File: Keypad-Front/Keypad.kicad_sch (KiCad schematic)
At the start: 64 parts, among them J1 RTC STEMMA QT, J3 JST-PH 6, J4 JST-PH 6, J5 JST-PH 8, J6 EXP QWIIC, J7 TOUCH QWIIC, U1 DS3231MZ, U2 LM1117-3.3, U3 CAP1214

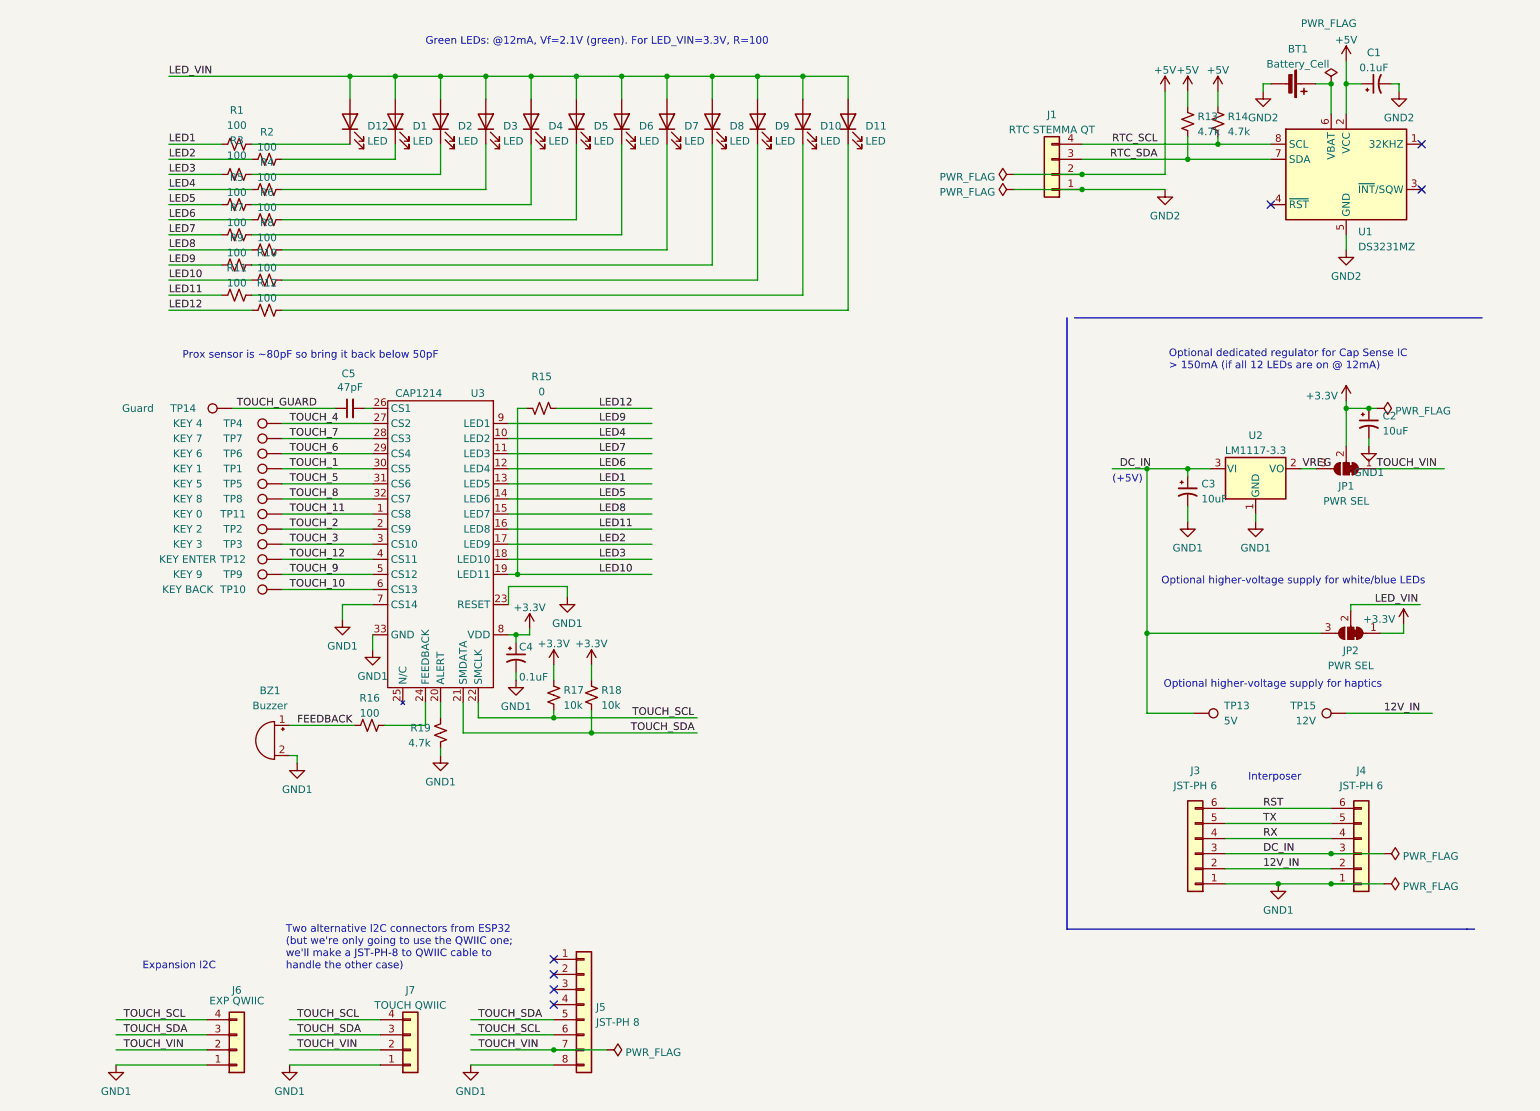
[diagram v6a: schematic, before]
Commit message: Fix some errors in original boards; add RFID functionality
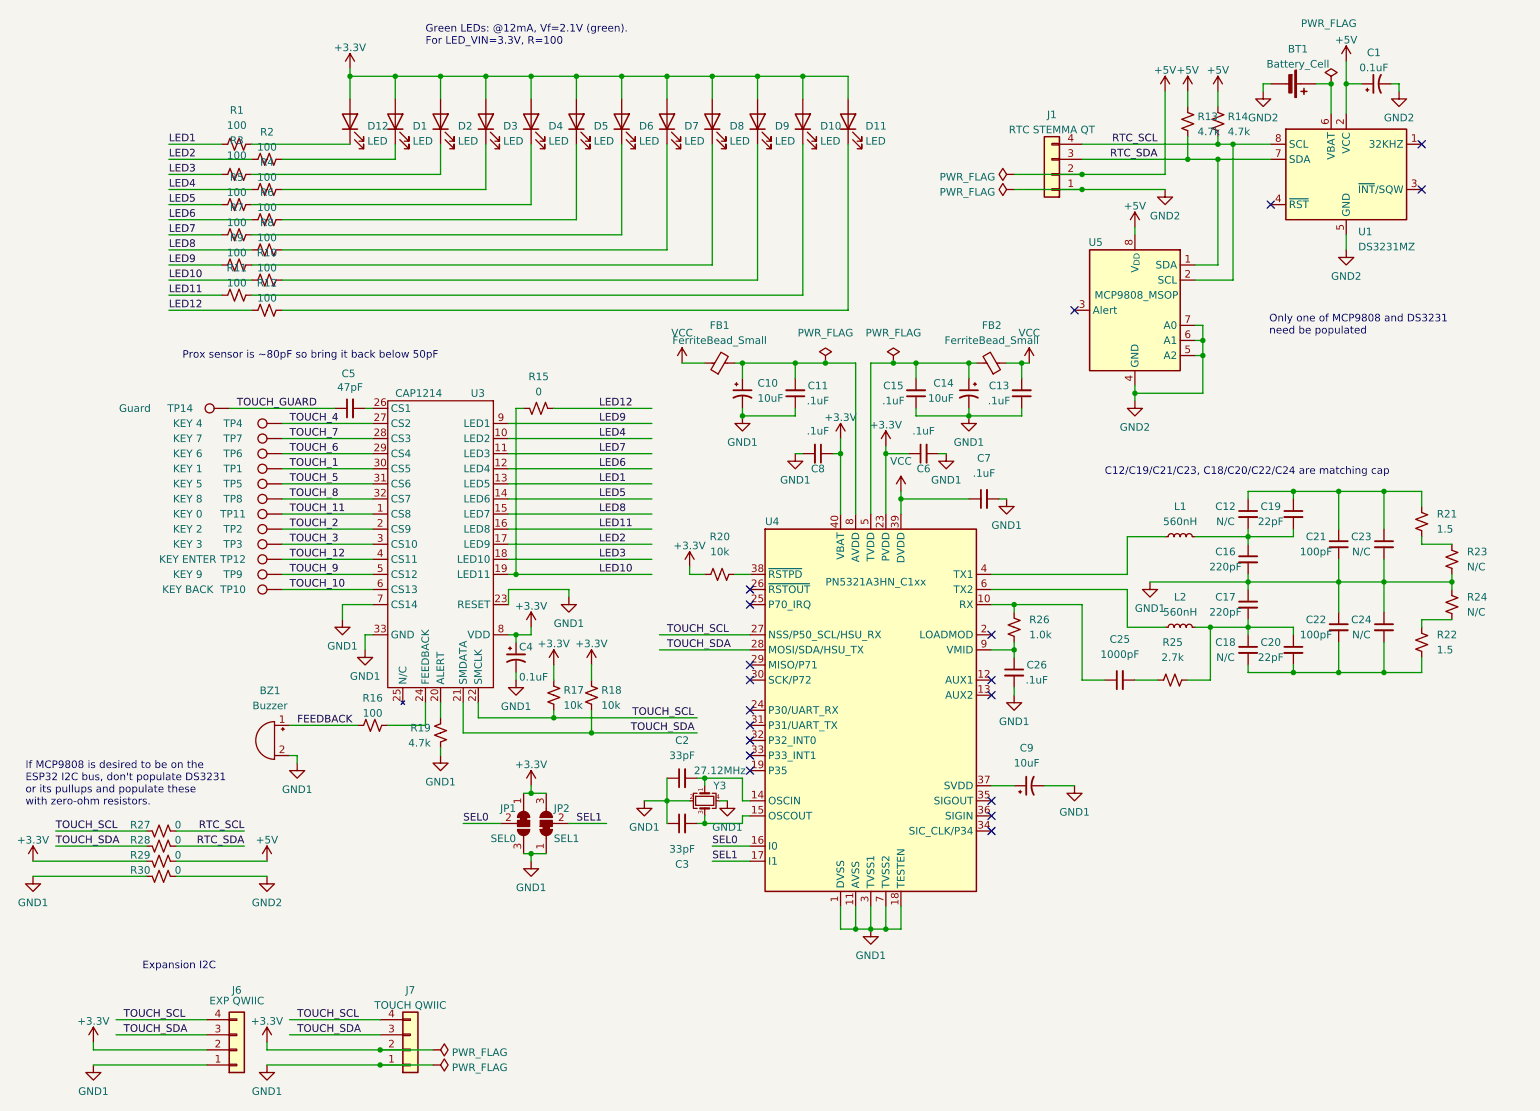
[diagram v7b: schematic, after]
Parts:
- removed C2, C3: 10uF, Capacitor_SMD:C_0805_2012Metric_Pad1.18x1.45mm_HandSolder, symbol Device:C_Polarized_Small_US
- removed J3, J4: JST-PH 6, Keypad:JST-PH-6-SMD, symbol Connector_Generic:Conn_01x06
- removed J5: JST-PH 8, symbol Connector_Generic:Conn_01x08
- removed TP13: 5V, TestPoint:TestPoint_Pad_2.0x2.0mm, symbol Connector:TestPoint
- removed TP15: 12V, TestPoint:TestPoint_Pad_2.0x2.0mm, symbol Connector:TestPoint
- removed U2: LM1117-3.3, Package_TO_SOT_SMD:SOT-223-3_TabPin2, symbol Regulator_Linear:LM1117-3.3
- added C10, C14, C9: 10uF, Capacitor_SMD:C_0805_2012Metric_Pad1.18x1.45mm_HandSolder, symbol Device:C_Polarized_Small_US
- added C11, C13, C15, C26, C6, C7, C8: .1uF, Capacitor_SMD:C_0805_2012Metric_Pad1.18x1.45mm_HandSolder, symbol Device:C_Small
- added C12, C18, C23, C24: N/C, Capacitor_SMD:C_0805_2012Metric_Pad1.18x1.45mm_HandSolder, symbol Device:C_Small
- added C16, C17: 220pF, Capacitor_SMD:C_0805_2012Metric_Pad1.18x1.45mm_HandSolder, symbol Device:C_Small
- added C19, C20: 22pF, Capacitor_SMD:C_0805_2012Metric_Pad1.18x1.45mm_HandSolder, symbol Device:C_Small
- added C2, C3: 33pF, Capacitor_SMD:C_0805_2012Metric_Pad1.18x1.45mm_HandSolder, symbol Device:C_Small
- added C21, C22: 100pF, Capacitor_SMD:C_0805_2012Metric_Pad1.18x1.45mm_HandSolder, symbol Device:C_Small
- added C25: 1000pF, Capacitor_SMD:C_0805_2012Metric_Pad1.18x1.45mm_HandSolder, symbol Device:C_Small
- added FB1, FB2: FerriteBead_Small, Resistor_SMD:R_0805_2012Metric_Pad1.20x1.40mm_HandSolder, symbol Device:FerriteBead_Small
- added L1, L2: 560nH, Inductor_SMD:L_0805_2012Metric_Pad1.15x1.40mm_HandSolder, symbol Device:L_Small
- added R20: 10k, Resistor_SMD:R_0805_2012Metric_Pad1.20x1.40mm_HandSolder, symbol Device:R_Small_US
- added R21, R22: 1.5, Resistor_SMD:R_0805_2012Metric_Pad1.20x1.40mm_HandSolder, symbol Device:R_Small_US
- added R23, R24: N/C, Jumper:SolderJumper-2_P1.3mm_Bridged_Pad1.0x1.5mm, symbol Device:R_Small_US
- added R25: 2.7k, Resistor_SMD:R_0805_2012Metric_Pad1.20x1.40mm_HandSolder, symbol Device:R_Small_US
- added R26: 1.0k, Resistor_SMD:R_0805_2012Metric_Pad1.20x1.40mm_HandSolder, symbol Device:R_Small_US
- added R27, R28, R29, R30: 0, Resistor_SMD:R_0805_2012Metric_Pad1.20x1.40mm_HandSolder, symbol Device:R_Small_US
- added U4: PN5321A3HN_C1xx, Package_DFN_QFN:HVQFN-40-1EP_6x6mm_P0.5mm_EP4.1x4.1mm, symbol RF_NFC:PN5321A3HN_C1xx
- added U5: MCP9808_MSOP, Package_SO:MSOP-8_3x3mm_P0.65mm, symbol Sensor_Temperature:MCP9808_MSOP
- added Y3: 27.12MHz, Crystal:Crystal_SMD_TXC_7M-4Pin_3.2x2.5mm_HandSoldering, symbol Device:Crystal_GND24_Small
- JP1: value PWR SEL -> SEL0; footprint Jumper:SolderJumper-3_P1.3mm_Bridged12_RoundedPad1.0x1.5mm -> Jumper:SolderJumper-3_P1.3mm_Bridged12_Pad1.0x1.5mm
- JP2: value PWR SEL -> SEL1; footprint Jumper:SolderJumper-3_P1.3mm_Bridged12_RoundedPad1.0x1.5mm -> Jumper:SolderJumper-3_P1.3mm_Bridged12_Pad1.0x1.5mm
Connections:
- net DC_IN is gone; now on net GND1: JP2.3 (B)
- net VREG is gone; now on net +3.3V: JP1.3 (B)
- net +3.3V: now also D1.2 (A), D10.2 (A), D11.2 (A), D12.2 (A), D2.2 (A), D3.2 (A), D4.2 (A), D5.2 (A), D6.2 (A), D7.2 (A), D8.2 (A), D9.2 (A), J6.2 (Pin_2), J7.2 (Pin_2), C6.1, C8.1, R20.1, R29.1, U4.23 (PVDD), U4.40 (VBAT); no longer JP1.2 (C)
- net +5V: now also R29.2, U5.8 (V_{DD})
- net GND1: now also JP1.1 (A), C10.2, C11.1, C13.1, C14.2, C15.1, C16.2, C17.1, C2.1, C21.2, C22.1, C23.2, C24.1, C26.2, C3.1, C6.2, C7.2, C8.2, C9.2, R23.1, R24.2, R30.1, U4.1 (DVSS), U4.11 (AVSS), U4.18 (TESTEN), U4.3 (TVSS1), U4.41 (AVSS), U4.7 (TVSS2), Y3.2, Y3.4
- net GND2: now also R30.2, U5.4 (GND), U5.5 (A2), U5.6 (A1), U5.7 (A0)
- net RTC_SCL: now also R27.2, U5.2 (SCL)
- net RTC_SDA: now also R28.2, U5.1 (SDA)
- net TOUCH_SCL: now also R27.1, U4.27 (NSS/P50_SCL/HSU_RX)
- net TOUCH_SDA: now also R28.1, U4.28 (MOSI/SDA/HSU_TX)
- removed net LED_VIN: D1.2 (A), D10.2 (A), D11.2 (A), D12.2 (A), D2.2 (A), D3.2 (A), D4.2 (A), D5.2 (A), D6.2 (A), D7.2 (A), D8.2 (A), D9.2 (A), JP2.2 (C)
- removed net TOUCH_VIN: J6.2 (Pin_2), J7.2 (Pin_2), JP1.1 (A)
- new net: C14.1, C15.2, FB2.2, U4.5 (TVDD)
- new net: C25.1, R26.2, U4.10 (RX)
- new net: C2.2, U4.14 (OSCIN), Y3.1
- new net: C3.2, U4.15 (OSCOUT), Y3.3
- new net: C9.1, U4.37 (SVDD)
- new net: R20.2, U4.38 (~{RSTPD})
- new net: L1.1, U4.4 (TX1)
- new net: L2.1, U4.6 (TX2)
- new net: C10.1, C11.2, FB1.2, U4.8 (AVDD)
- new net: C26.1, R26.1, U4.9 (VMID)
- new net: R21.1, R23.2
- new net: C12.1, C19.1, C21.1, C23.1, R21.2
- new net: C17.2, C18.1, C20.1, L2.2, R25.1
- new net: C25.2, R25.2
- new net: C12.2, C16.1, C19.2, L1.2
- new net: C18.2, C20.2, C22.2, C24.2, R22.1
- new net: R22.2, R24.1
- new net SEL0: JP2.2 (C), U4.16 (I0)
- new net SEL1: JP1.2 (C), U4.17 (I1)
- new net VCC: C13.2, C7.1, FB1.1, FB2.1, U4.39 (DVDD)
- no-connect marks 7 -> 19
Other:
- note added: "C12/C19/C21/C23, C18/C20/C22/C24 are matching cap"
- note added: "If MCP9808 is desired to be on the ESP32 I2C bus, don't populate DS3231 or its pullups and populate these with zero-ohm resistors."
- note added: "Only one of MCP9808 and DS3231 need be populated"
- note removed: "(+5V)"
- note removed: "Interposer"
- note removed: "Optional dedicated regulator for Cap Sense IC > 150mA (if all 12 LEDs are on @ 12mA)"
- note removed: "Optional higher-voltage supply for haptics"
- note removed: "Optional higher-voltage supply for white/blue LEDs"
- note removed: "Two alternative I2C connectors from ESP32 (but we're only going to use the QWIIC one; we'll make a JST-PH-8 to QWIIC cable to handle the other case)"
- moved on the sheet: R15, R16, TP14

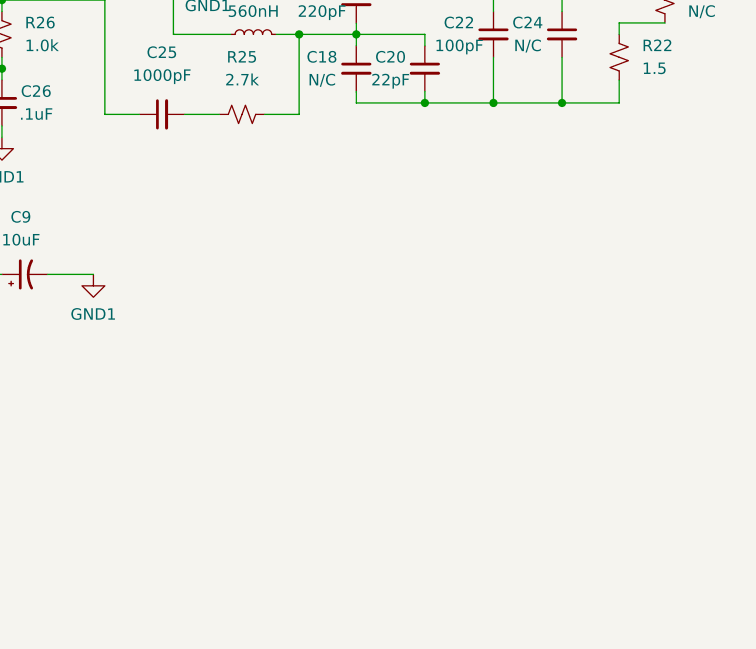
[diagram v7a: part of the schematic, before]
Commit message: Add PCA9536 I/O expander to handle LED12 and hardware version detect
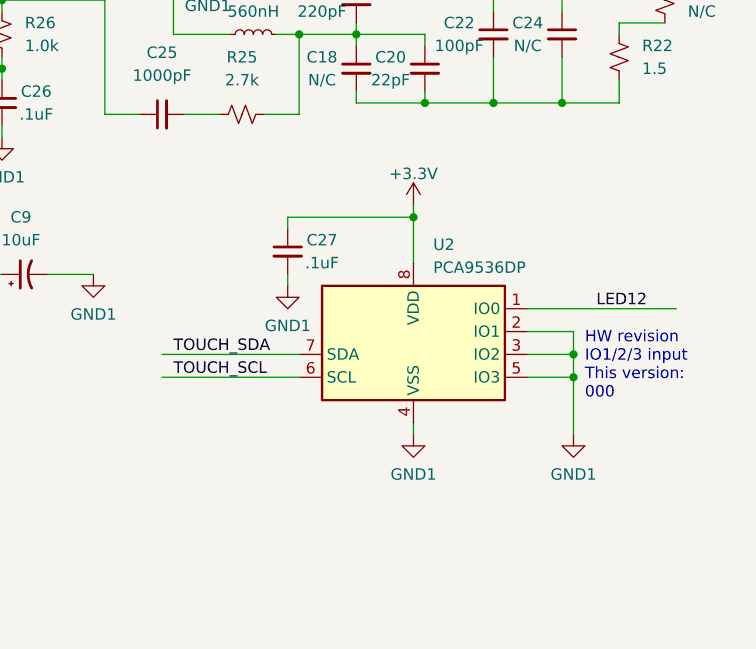
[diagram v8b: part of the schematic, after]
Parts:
- added C27: .1uF, Capacitor_SMD:C_0805_2012Metric_Pad1.18x1.45mm_HandSolder, symbol Device:C_Small
- added U2: PCA9536DP, Package_SO:TSSOP-8_3x3mm_P0.65mm, symbol Interface_Expansion:PCA9536DP
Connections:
- net +3.3V: now also C27.1, U2.8 (VDD)
- net GND1: now also C27.2, U2.2 (IO1), U2.3 (IO2), U2.4 (VSS), U2.5 (IO3)
- net LED12: now also U2.1 (IO0)
- net TOUCH_SCL: now also U2.6 (SCL)
- net TOUCH_SDA: now also U2.7 (SDA)
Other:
- note added: "HW revision IO1/2/3 input This version: 000"
